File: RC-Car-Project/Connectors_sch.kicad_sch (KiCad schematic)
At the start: 6 parts, among them J1 MCU_IF, J3 MOTOR_IF, J4 BATT_1, J5 MISC_IF, J6 ANT_IF, J7 BATT2

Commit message: Connector stuff
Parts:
- J1: footprint (none) -> Connector_PinHeader_2.54mm:PinHeader_2x04_P2.54mm_Vertical
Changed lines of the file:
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@@
 			)
 		)
-		(property "Footprint" ""
+		(property "Footprint" "Connector_PinHeader_2.54mm:PinHeader_2x04_P2.54mm_Vertical"
 			(at 115.57 100.33 0)
 			(effects

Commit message: Added footprints + final parts. (Need to finish buck converter next)
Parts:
- J5: footprint (none) -> Connector_PinHeader_2.54mm:PinHeader_2x04_P2.54mm_Vertical
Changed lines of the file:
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@@
 			)
 		)
-		(property "Footprint" ""
+		(property "Footprint" "Connector_PinHeader_2.54mm:PinHeader_2x04_P2.54mm_Vertical"
 			(at 223.52 97.79 0)
 			(effects

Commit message: Finished Buck
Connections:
- net GNDA: now reaches J5.2 (Pin_2)
- net GNDA: now also J5.5 (Pin_5)
- no-connect marks 7 -> 5
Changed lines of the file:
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@@
-	)
-	(no_connect
-		(at 218.44 92.71)
 	)
 	(no_connect
@@
 	)
 	(no_connect
-		(at 218.44 100.33)
-	)
-	(no_connect
 		(at 218.44 90.17)
 	)
@@
 			)
 			(justify right)
+		)
+	)
+	(symbol
+		(lib_id "power:GNDA")
+		(at 218.44 92.71 270)
+		(unit 1)
+		(exclude_from_sim no)
+		(in_bom yes)
+		(on_board yes)
+		(dnp no)
+		(fields_autoplaced yes)
+		(property "Reference" "#PWR013"
+			(at 212.09 92.71 0)
+			(effects
+				(font
+					(size 1.27 1.27)
+				)
+				(hide yes)
+			)
+		)
+		(property "Value" "GNDA"
+			(at 214.63 92.7099 90)
+			(effects
+				(font
+					(size 1.27 1.27)
+				)
+				(justify right)
+			)
+		)
+		(property "Footprint" ""
+			(at 218.44 92.71 0)
+			(effects
+				(font
+					(size 1.27 1.27)
+				)
+				(hide yes)
+			)
+		)
+		(property "Datasheet" ""
+			(at 218.44 92.71 0)
+			(effects
+				(font
+					(size 1.27 1.27)
+				)
+				(hide yes)
+			)
+		)
+		(property "Description" "Power symbol creates a global label with name \"GNDA\" , analog ground"
+			(at 218.44 92.71 0)
+			(effects
+				(font
+					(size 1.27 1.27)
+				)
+				(hide yes)
+			)
+		)
+		(pin "1"
+		)
+		(instances
+			(project "RC-Car-Project"
+				(path "/ba870fd1-751d-4755-8e1a-1ea86ca9e2f6/47812da9-b622-4bda-8507-4e09448e1ff5"
+					(reference "#PWR013")
+					(unit 1)
+				)
+			)
 		)
 	)
@@
 					(unit 1)
 				)
+			)
+		)
+	)
+	(symbol
+		(lib_id "power:GNDA")
+		(at 218.44 100.33 270)
+		(unit 1)
+		(exclude_from_sim no)
+		(in_bom yes)
+		(on_board yes)
+		(dnp no)
+		(fields_autoplaced yes)
+		(property "Reference" "#PWR012"
+			(at 212.09 100.33 0)
+			(effects
+				(font
+					(size 1.27 1.27)
+				)
+				(hide yes)
+			)
+		)
+		(property "Value" "GNDA"
+			(at 214.63 100.3299 90)
+			(effects
+				(font
+					(size 1.27 1.27)
+				)
+				(justify right)
+			)
+		)
+		(property "Footprint" ""
+			(at 218.44 100.33 0)
+			(effects
+				(font
+					(size 1.27 1.27)
+				)
+				(hide yes)
+			)
+		)
+		(property "Datasheet" ""
+			(at 218.44 100.33 0)
+			(effects
+				(font
+					(size 1.27 1.27)
+				)
+				(hide yes)
+			)
+		)
+		(property "Description" "Power symbol creates a global label with name \"GNDA\" , analog ground"
+			(at 218.44 100.33 0)
+			(effects
+				(font
+					(size 1.27 1.27)
+				)
+				(hide yes)
+			)
+		)
+		(pin "1"
+		)
+		(instances
+			(project "RC-Car-Project"
+				(path "/ba870fd1-751d-4755-8e1a-1ea86ca9e2f6/47812da9-b622-4bda-8507-4e09448e1ff5"
+					(reference "#PWR012")
+					(unit 1)
+				)

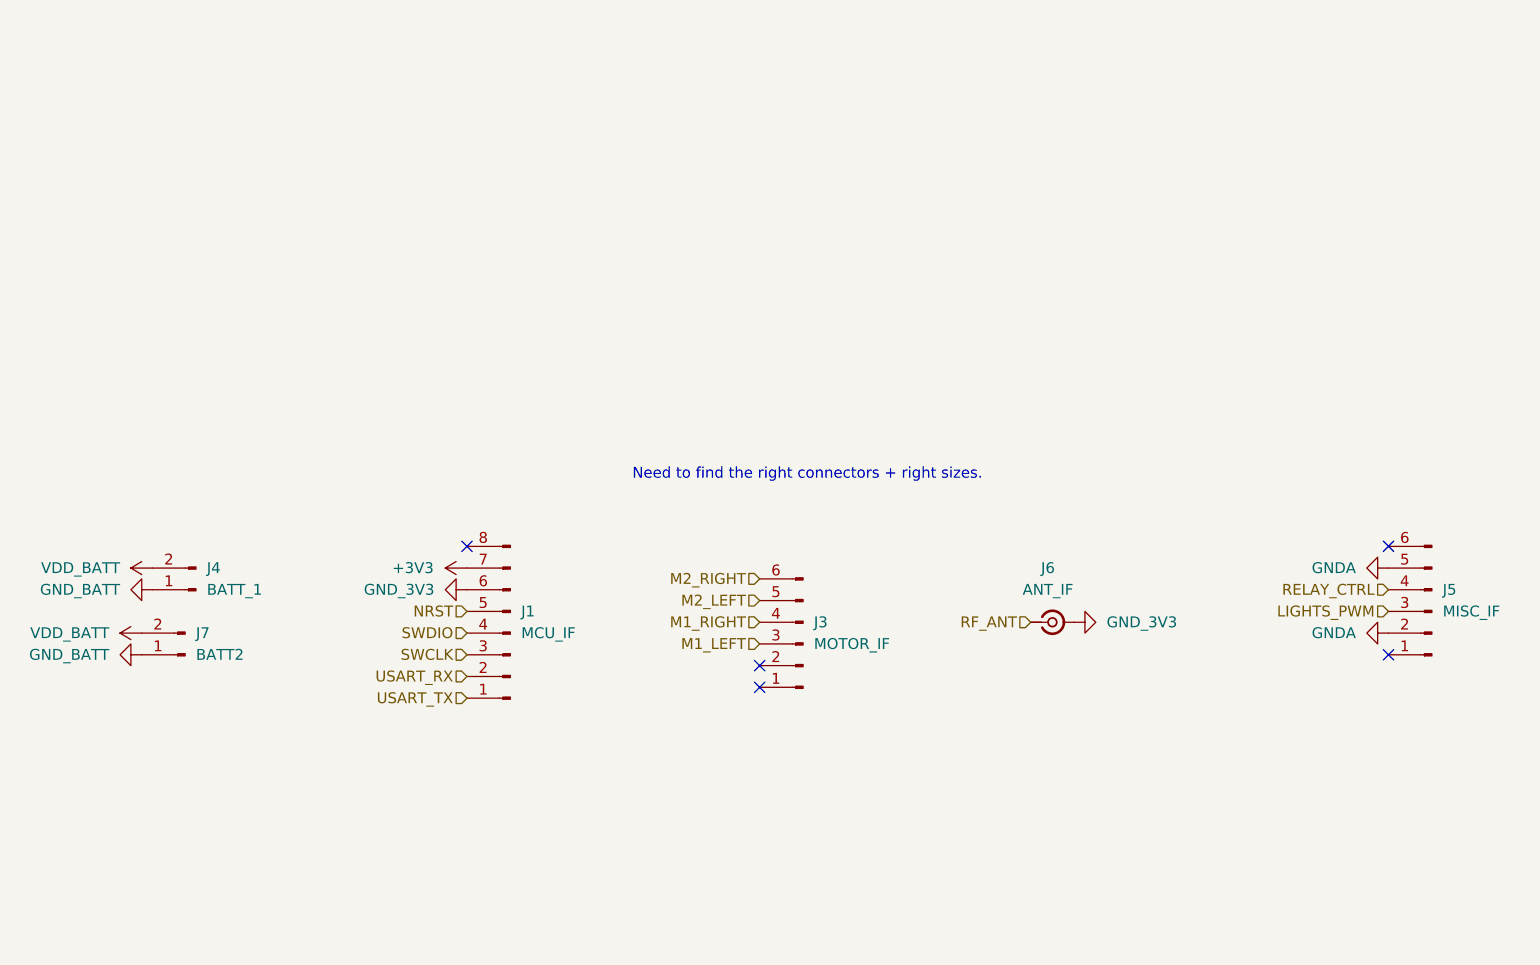
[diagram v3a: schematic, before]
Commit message: Added XT60 Connectors
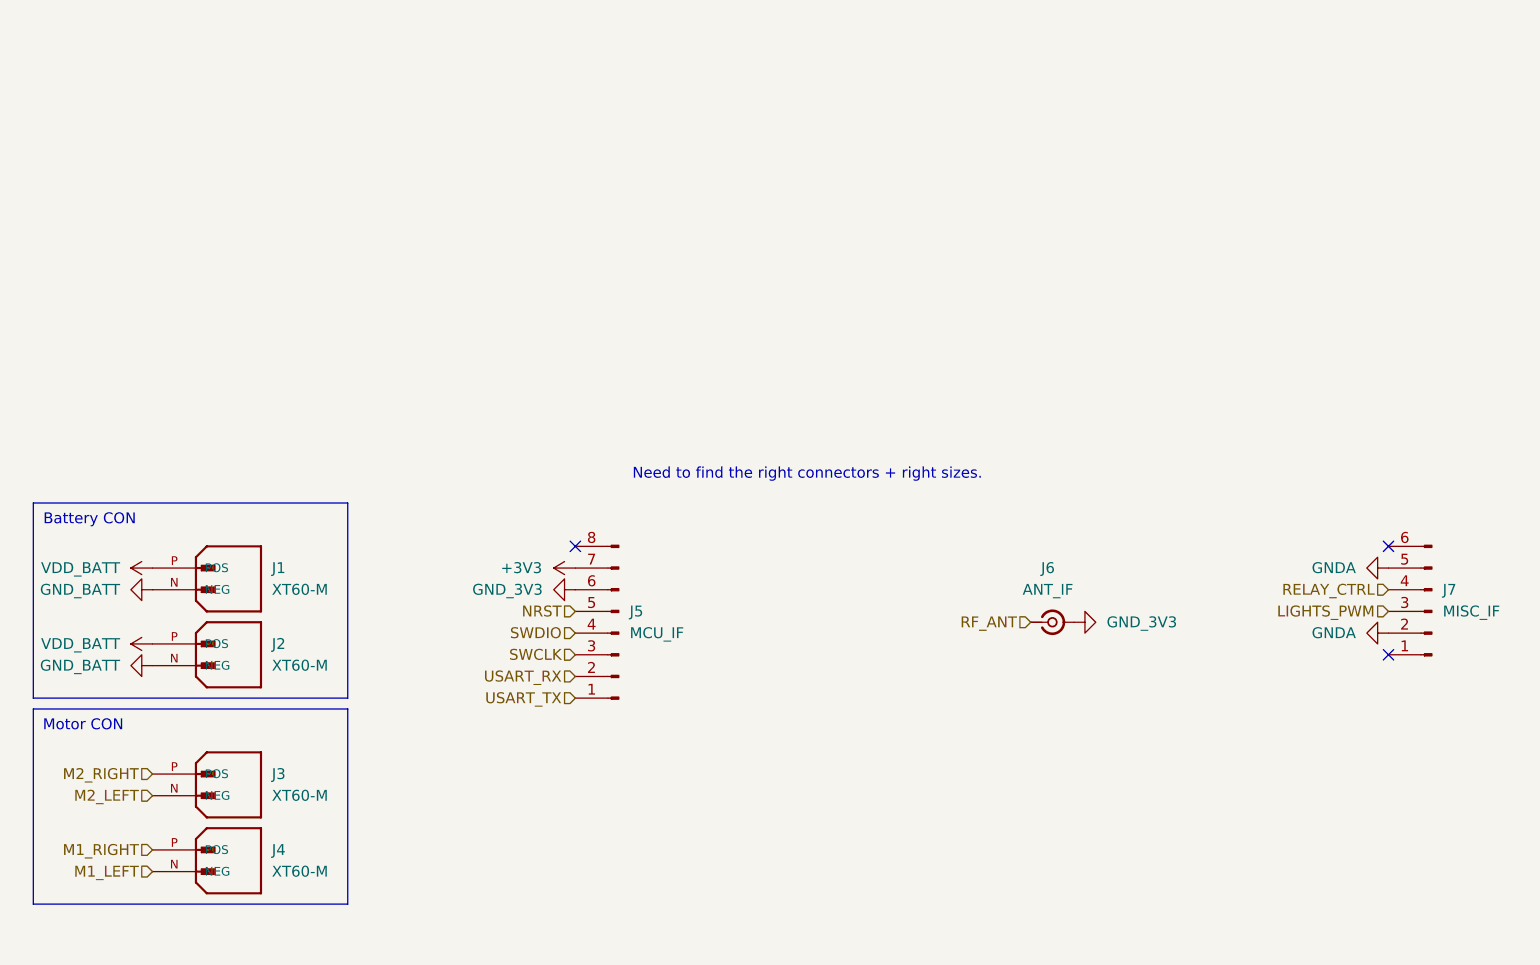
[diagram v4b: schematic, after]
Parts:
- removed J3: MOTOR_IF, symbol Connector:Conn_01x06_Pin
- removed J4: BATT_1, footprints:CONN_1805375_RSP, symbol Connector:Conn_01x02_Pin
- removed J7: BATT2, footprints:CONN_1805375_RSP, symbol Connector:Conn_01x02_Pin
- added J1, J2, J3, J4: XT60-M, symbol XT60-M:XT60-M
- renumbered J1 to J5, J5 to J7
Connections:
- net GND_BATT: now also J1.N (NEG), J2.N (NEG)
- net M1_LEFT: now also J4.N (NEG)
- net M1_RIGHT: now also J4.P (POS)
- net M2_LEFT: now also J3.N (NEG)
- net M2_RIGHT: now also J3.P (POS)
- net VDD_BATT: now also J1.P (POS), J2.P (POS)
- no-connect marks 5 -> 3
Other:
- note added: "Battery CON"
- note added: "Motor CON"
- moved on the sheet: J5

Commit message: Add thermo adc and camera
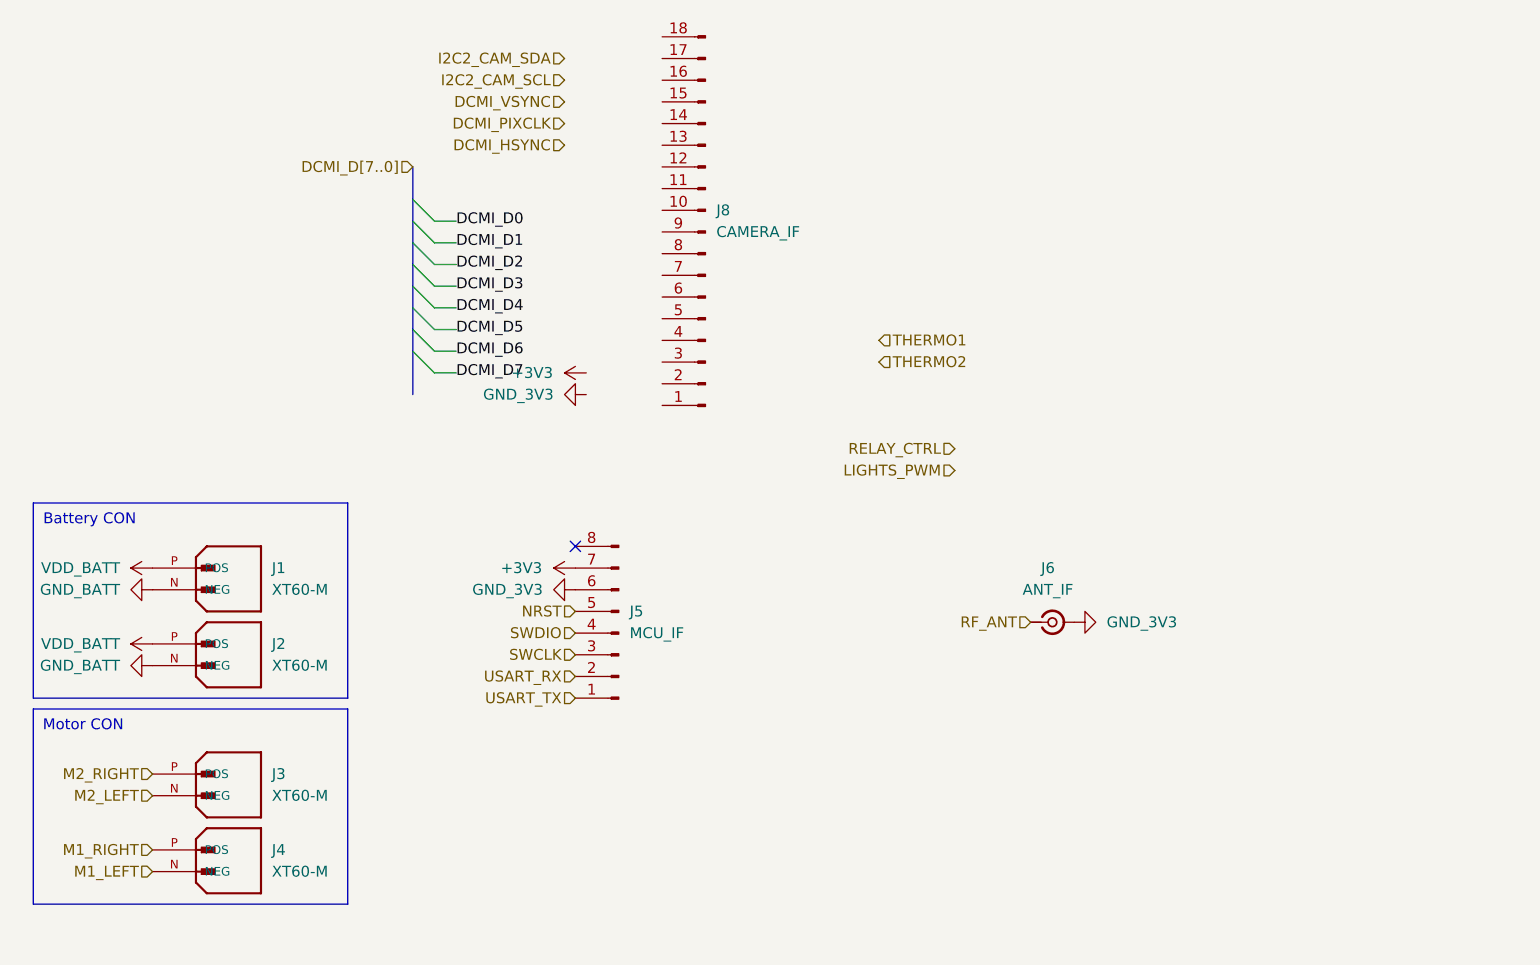
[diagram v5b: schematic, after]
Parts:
- removed J7: MISC_IF, Connector_PinHeader_2.54mm:PinHeader_2x04_P2.54mm_Vertical, symbol Connector:Conn_01x06_Pin
- added J8: CAMERA_IF, symbol Connector:Conn_01x18_Pin
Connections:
- no-connect marks 3 -> 1
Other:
- note removed: "Need to find the right connectors + right sizes."

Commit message: Added Camera Connector, Minor Controller Fixes
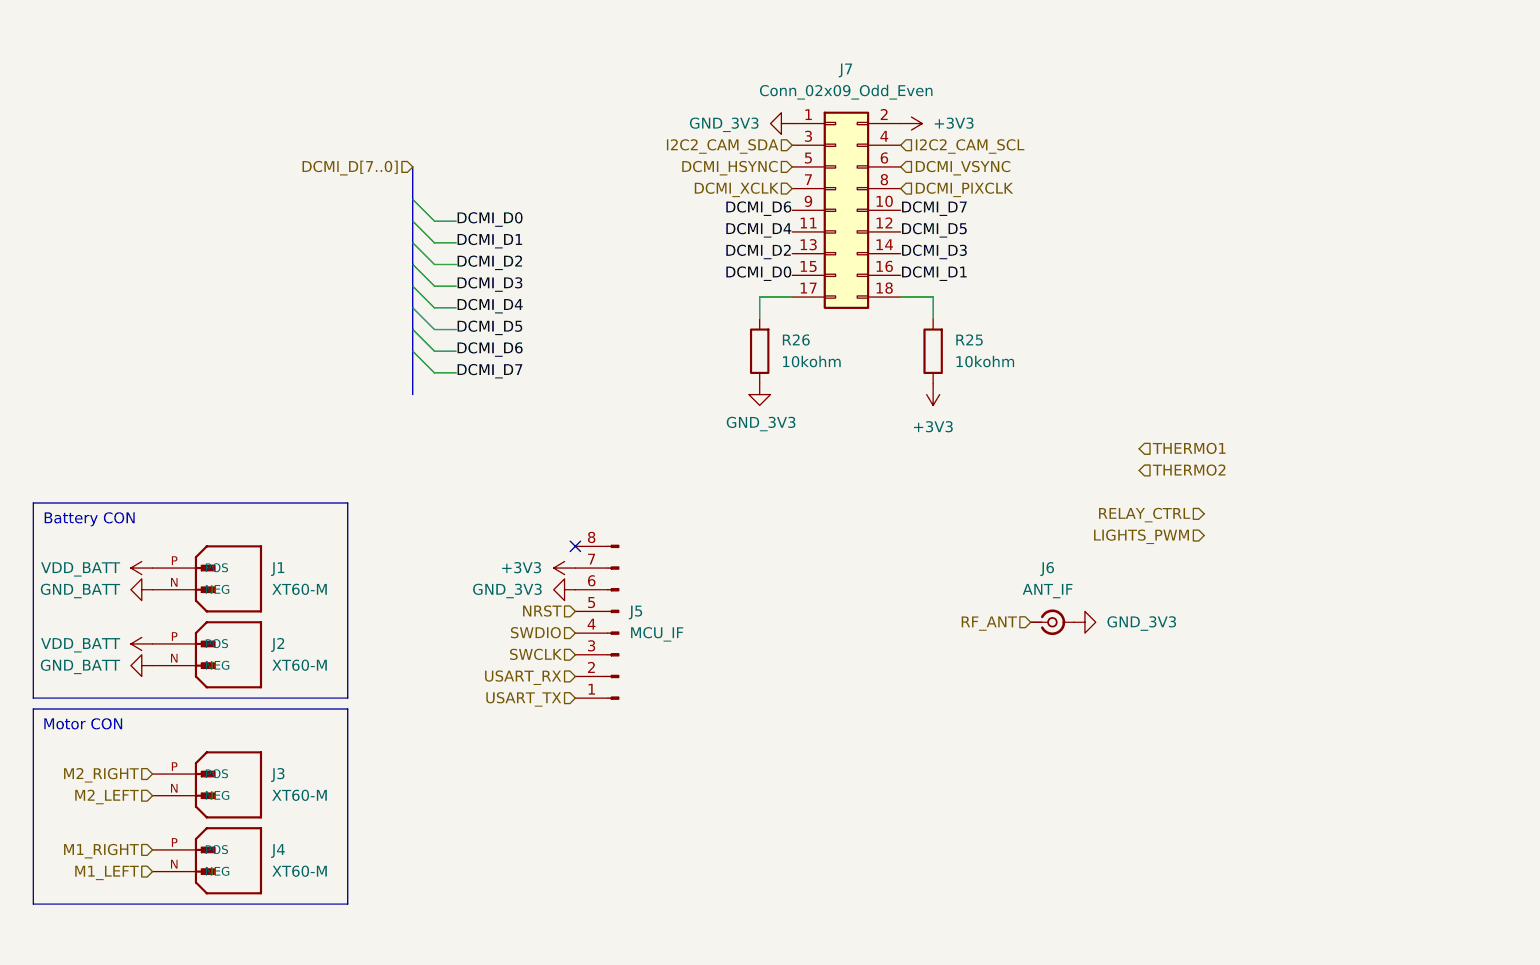
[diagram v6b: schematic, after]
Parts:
- removed J8: CAMERA_IF, symbol Connector:Conn_01x18_Pin
- added J7: Conn_02x09_Odd_Even, Connector_PinSocket_2.54mm:PinSocket_2x09_P2.54mm_Horizontal, symbol Connector_Generic:Conn_02x09_Odd_Even
- added R25, R26: 10kohm, Resistor_SMD:R_0201_0603Metric, symbol Device:R
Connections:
- net +3V3: now also J7.2 (Pin_2), R25.1
- net DCMI_D0: now also J7.15 (Pin_15)
- net DCMI_D1: now also J7.16 (Pin_16)
- net DCMI_D2: now also J7.13 (Pin_13)
- net DCMI_D3: now also J7.14 (Pin_14)
- net DCMI_D4: now also J7.11 (Pin_11)
- net DCMI_D5: now also J7.12 (Pin_12)
- net DCMI_D6: now also J7.9 (Pin_9)
- net DCMI_D7: now also J7.10 (Pin_10)
- net DCMI_HSYNC: now also J7.5 (Pin_5)
- net DCMI_PIXCLK: now also J7.8 (Pin_8)
- net DCMI_VSYNC: now also J7.6 (Pin_6)
- net GND_3V3: now also J7.1 (Pin_1), R26.1
- net I2C2_CAM_SCL: now also J7.4 (Pin_4)
- net I2C2_CAM_SDA: now also J7.3 (Pin_3)
- new net: J7.17 (Pin_17), R26.2
- new net: J7.18 (Pin_18), R25.2
- new net DCMI_XCLK: J7.7 (Pin_7)

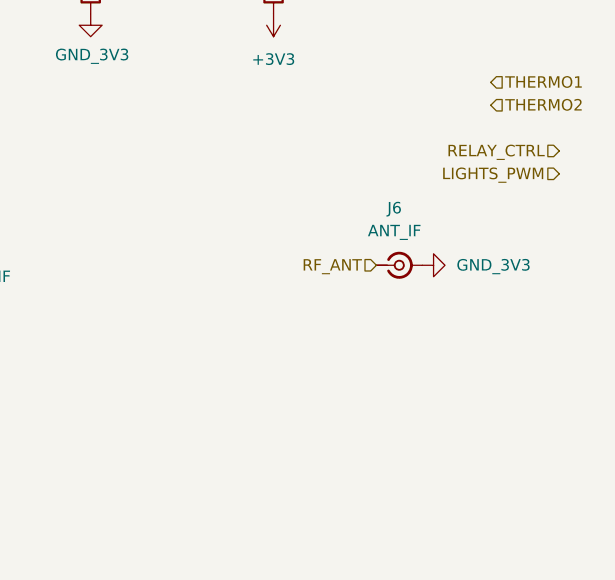
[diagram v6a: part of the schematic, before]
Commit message: Added LED Driver
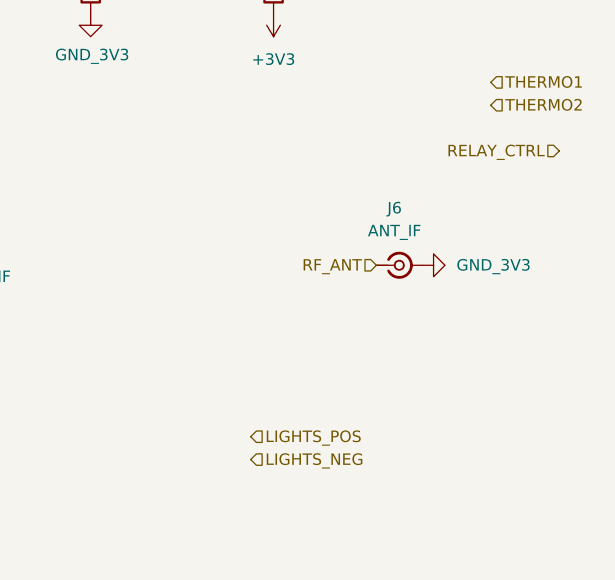
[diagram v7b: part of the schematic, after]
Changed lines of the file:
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@@
-		)
-	)
-	(hierarchical_label "LIGHTS_PWM"
-		(shape input)
-		(at 196.85 88.9 180)
-		(fields_autoplaced yes)
-		(effects
-			(font
-				(size 1.27 1.27)
-			)
-			(justify right)
 		)
 	)
@@
 		)
 	)
+	(hierarchical_label "LIGHTS_POS"
+		(shape input)
+		(at 162.56 118.11 0)
+		(fields_autoplaced yes)
+		(effects
+			(font
+				(size 1.27 1.27)
+			)
+			(justify left)
+		)
+	)
 	(hierarchical_label "THERMO1"
 		(shape input)
@@
 		)
 	)
+	(hierarchical_label "LIGHTS_NEG"
+		(shape input)
+		(at 162.56 120.65 0)
+		(fields_autoplaced yes)
+		(effects
+			(font
+				(size 1.27 1.27)
+			)
+			(justify left)
+		)
+	)

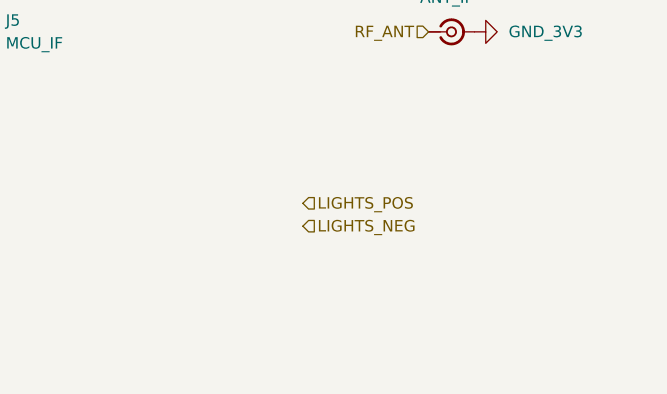
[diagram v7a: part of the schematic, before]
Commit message: Fixed LED Drivers
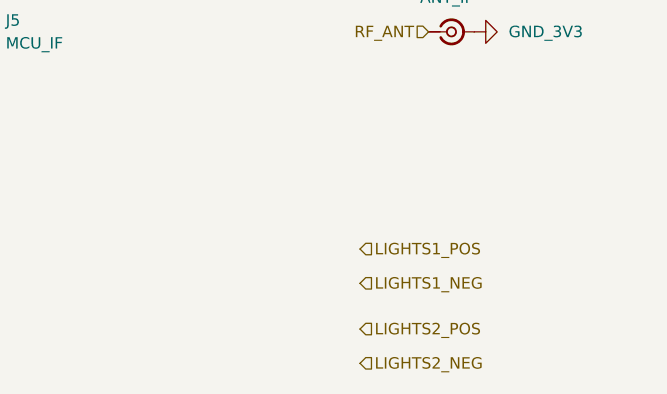
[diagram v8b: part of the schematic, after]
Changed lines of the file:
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@@
+		)
+	)
+	(hierarchical_label "LIGHTS2_NEG"
+		(shape input)
+		(at 168.91 135.89 0)
+		(fields_autoplaced yes)
+		(effects
+			(font
+				(size 1.27 1.27)
+			)
+			(justify left)
 		)
 	)
@@
 			)
 			(justify right)
+		)
+	)
+	(hierarchical_label "LIGHTS1_NEG"
+		(shape input)
+		(at 168.91 127 0)
+		(fields_autoplaced yes)
+		(effects
+			(font
+				(size 1.27 1.27)
+			)
+			(justify left)
 		)
 	)
@@
 		)
 	)
-	(hierarchical_label "LIGHTS_POS"
-		(shape input)
-		(at 162.56 118.11 0)
-		(fields_autoplaced yes)
-		(effects
-			(font
-				(size 1.27 1.27)
-			)
-			(justify left)
-		)
-	)
 	(hierarchical_label "THERMO1"
 		(shape input)
@@
 		)
 	)
-	(hierarchical_label "LIGHTS_NEG"
+	(hierarchical_label "LIGHTS1_POS"
 		(shape input)
-		(at 162.56 120.65 0)
+		(at 168.91 123.19 0)
 		(fields_autoplaced yes)
 		(effects
+			(font
+				(size 1.27 1.27)
+			)
+			(justify left)
+		)
+	)
+	(hierarchical_label "LIGHTS2_POS"
+		(shape input)
+		(at 168.91 132.08 0)
+		(fields_autoplaced yes)
+		(effects
